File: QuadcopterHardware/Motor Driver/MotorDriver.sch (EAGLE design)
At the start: 4 parts

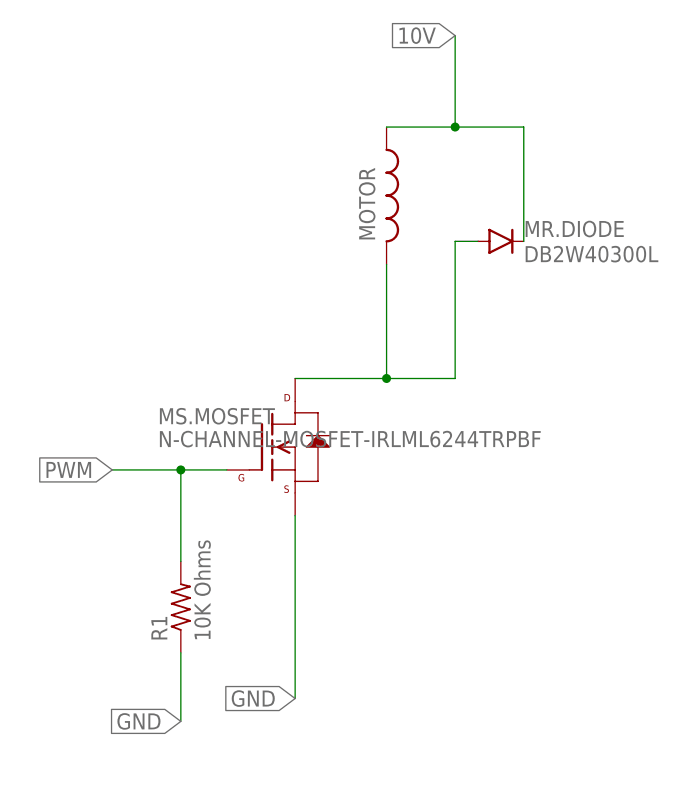
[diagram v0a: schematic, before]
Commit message: Update to MotorDriver schematic
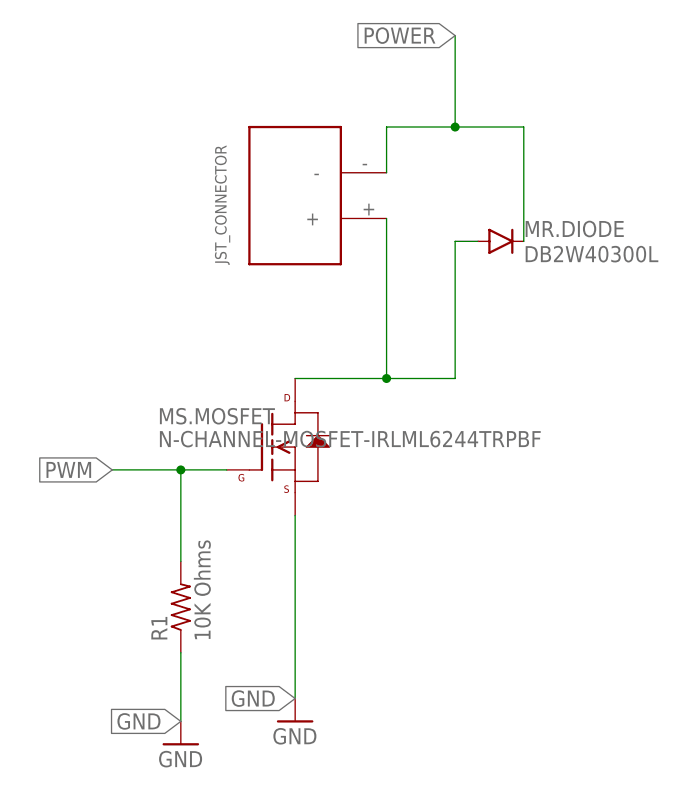
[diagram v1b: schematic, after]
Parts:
- MOTOR: value (none) -> JST_CONNECTOR_FEMALE; device rcl:L-USCEP125 -> quad:JST_CONNECTOR_FEMALE
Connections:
- removed net 10V: MOTOR.1, MR.DIODE.GPIN
- new net POWER: MOTOR.-, MR.DIODE.GPIN
- net DRAIN: now also MOTOR.+; no longer MOTOR.2
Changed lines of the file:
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@@
 <part name="MS.MOSFET" library="quad" deviceset="N-CHANNEL-MOSFET" device="-IRLML6244TRPBF"/>
 <part name="MR.DIODE" library="quad" deviceset="DB2W40300L" device=""/>
-<part name="MOTOR" library="rcl" deviceset="L-US" device="CEP125"/>
 <part name="R1" library="rcl" deviceset="R-US_" device="0204/5" value="10K Ohms"/>
+<part name="GND1" library="SparkFun-Aesthetics" deviceset="GND" device=""/>
+<part name="GND2" library="SparkFun-Aesthetics" deviceset="GND" device=""/>
+<part name="MOTOR" library="quad" deviceset="JST_CONNECTOR_FEMALE" device=""/>
 </parts>
 <sheets>
@@
 <instance part="MS.MOSFET" gate="G$1" x="5.08" y="48.26"/>
 <instance part="MR.DIODE" gate="G$1" x="30.48" y="71.12"/>
-<instance part="MOTOR" gate="G$1" x="17.78" y="76.2"/>
 <instance part="R1" gate="G$1" x="-5.08" y="30.48" rot="R90"/>
+<instance part="GND1" gate="1" x="7.62" y="17.78"/>
+<instance part="GND2" gate="1" x="-5.08" y="15.24"/>
+<instance part="MOTOR" gate="G$1" x="7.62" y="76.2" rot="R90"/>
 </instances>
 <busses>
@@
 <segment>
 <pinref part="MS.MOSFET" gate="G$1" pin="D"/>
-<pinref part="MOTOR" gate="G$1" pin="2"/>
 <wire x1="7.62" y1="55.88" x2="17.78" y2="55.88" width="0.1524" layer="91"/>
-<wire x1="17.78" y1="55.88" x2="17.78" y2="68.58" width="0.1524" layer="91"/>
+<wire x1="17.78" y1="55.88" x2="17.78" y2="73.66" width="0.1524" layer="91"/>
 <pinref part="MR.DIODE" gate="G$1" pin="PPIN"/>
 <wire x1="27.94" y1="71.12" x2="25.4" y2="71.12" width="0.1524" layer="91"/>
@@
 <wire x1="25.4" y1="55.88" x2="17.78" y2="55.88" width="0.1524" layer="91"/>
 <junction x="17.78" y="55.88"/>
+<pinref part="MOTOR" gate="G$1" pin="+"/>
 </segment>
 </net>
-<net name="10V" class="0">
+<net name="POWER" class="0">
 <segment>
-<pinref part="MOTOR" gate="G$1" pin="1"/>
 <wire x1="17.78" y1="83.82" x2="25.4" y2="83.82" width="0.1524" layer="91"/>
 <pinref part="MR.DIODE" gate="G$1" pin="GPIN"/>
@@
 <junction x="25.4" y="83.82"/>
 <label x="25.4" y="93.98" size="1.778" layer="95" rot="R180" xref="yes"/>
+<pinref part="MOTOR" gate="G$1" pin="-"/>
+<wire x1="17.78" y1="83.82" x2="17.78" y2="78.74" width="0.1524" layer="91"/>
 </segment>
 </net>
@@
 <wire x1="-5.08" y1="25.4" x2="-5.08" y2="17.78" width="0.1524" layer="91"/>
 <label x="-5.08" y="17.78" size="1.778" layer="95" rot="R180" xref="yes"/>
+<pinref part="GND2" gate="1" pin="GND"/>
 </segment>
 <segment>
@@
 <wire x1="7.62" y1="40.64" x2="7.62" y2="20.32" width="0.1524" layer="91"/>
 <label x="7.62" y="20.32" size="1.778" layer="95" rot="R180" xref="yes"/>
+<pinref part="GND1" gate="1" pin="GND"/>
 </segment>
 </net>

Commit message: Updated MotorDriver to Version 3
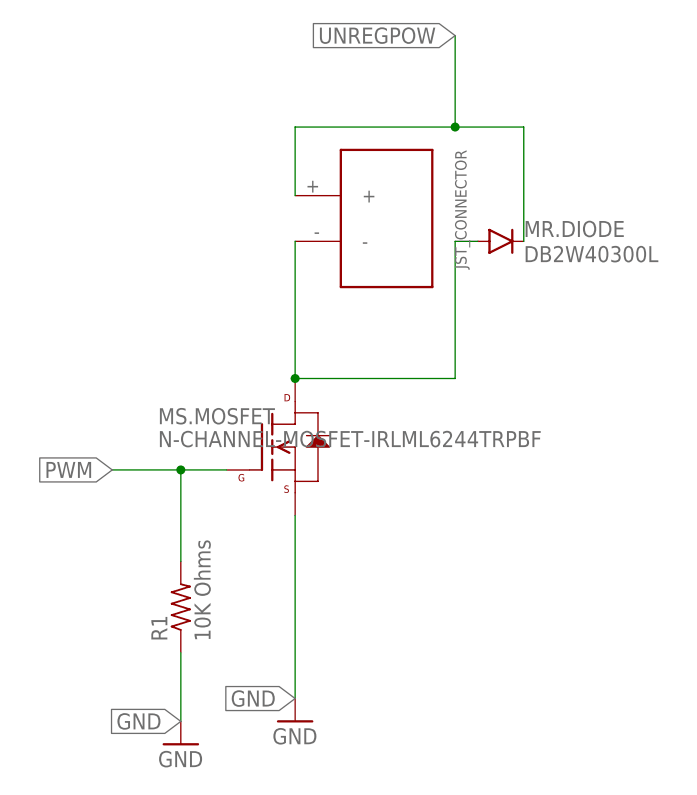
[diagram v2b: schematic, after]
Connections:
- removed net POWER: MOTOR.-, MR.DIODE.GPIN
- new net UNREGPOW: MOTOR.+, MR.DIODE.GPIN
- net DRAIN: now also MOTOR.-; no longer MOTOR.+
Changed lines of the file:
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@@
 <instance part="GND1" gate="1" x="7.62" y="17.78"/>
 <instance part="GND2" gate="1" x="-5.08" y="15.24"/>
-<instance part="MOTOR" gate="G$1" x="7.62" y="76.2" rot="R90"/>
+<instance part="MOTOR" gate="G$1" x="17.78" y="73.66" rot="R270"/>
 </instances>
 <busses>
@@
 <segment>
 <pinref part="MS.MOSFET" gate="G$1" pin="D"/>
-<wire x1="7.62" y1="55.88" x2="17.78" y2="55.88" width="0.1524" layer="91"/>
-<wire x1="17.78" y1="55.88" x2="17.78" y2="73.66" width="0.1524" layer="91"/>
+<wire x1="7.62" y1="55.88" x2="25.4" y2="55.88" width="0.1524" layer="91"/>
 <pinref part="MR.DIODE" gate="G$1" pin="PPIN"/>
 <wire x1="27.94" y1="71.12" x2="25.4" y2="71.12" width="0.1524" layer="91"/>
 <wire x1="25.4" y1="71.12" x2="25.4" y2="55.88" width="0.1524" layer="91"/>
-<wire x1="25.4" y1="55.88" x2="17.78" y2="55.88" width="0.1524" layer="91"/>
-<junction x="17.78" y="55.88"/>
-<pinref part="MOTOR" gate="G$1" pin="+"/>
+<pinref part="MOTOR" gate="G$1" pin="-"/>
+<wire x1="7.62" y1="71.12" x2="7.62" y2="55.88" width="0.1524" layer="91"/>
+<junction x="7.62" y="55.88"/>
 </segment>
 </net>
-<net name="POWER" class="0">
+<net name="UNREGPOW" class="0">
 <segment>
-<wire x1="17.78" y1="83.82" x2="25.4" y2="83.82" width="0.1524" layer="91"/>
 <pinref part="MR.DIODE" gate="G$1" pin="GPIN"/>
 <wire x1="25.4" y1="83.82" x2="33.02" y2="83.82" width="0.1524" layer="91"/>
@@
 <junction x="25.4" y="83.82"/>
 <label x="25.4" y="93.98" size="1.778" layer="95" rot="R180" xref="yes"/>
-<pinref part="MOTOR" gate="G$1" pin="-"/>
-<wire x1="17.78" y1="83.82" x2="17.78" y2="78.74" width="0.1524" layer="91"/>
+<pinref part="MOTOR" gate="G$1" pin="+"/>
+<wire x1="25.4" y1="83.82" x2="7.62" y2="83.82" width="0.1524" layer="91"/>
+<wire x1="7.62" y1="83.82" x2="7.62" y2="76.2" width="0.1524" layer="91"/>
 </segment>
 </net>
